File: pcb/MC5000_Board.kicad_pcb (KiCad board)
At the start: 2 copper layers, 100 x 97.5 mm, 127 parts, among them J1 USB_B_Micro, J14 Conn_01x04_Female, J15 Conn_01x04_Female, J16 Conn_01x04_Female, J17 Conn_01x04_Female, J18 Conn_01x04_Female, J19 Conn_01x04_Female, J2 Conn_01x04_Male, J20 Conn_01x04_Female, J21 Conn_01x04_Female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

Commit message: Fabrication stuff
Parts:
- BZ1: footprint Buzzer_Beeper:MagneticBuzzer_CUI_CMT-8504-100-SMT -> LCSC_parts:MagneticBuzzer_7.5x7.5_SMT

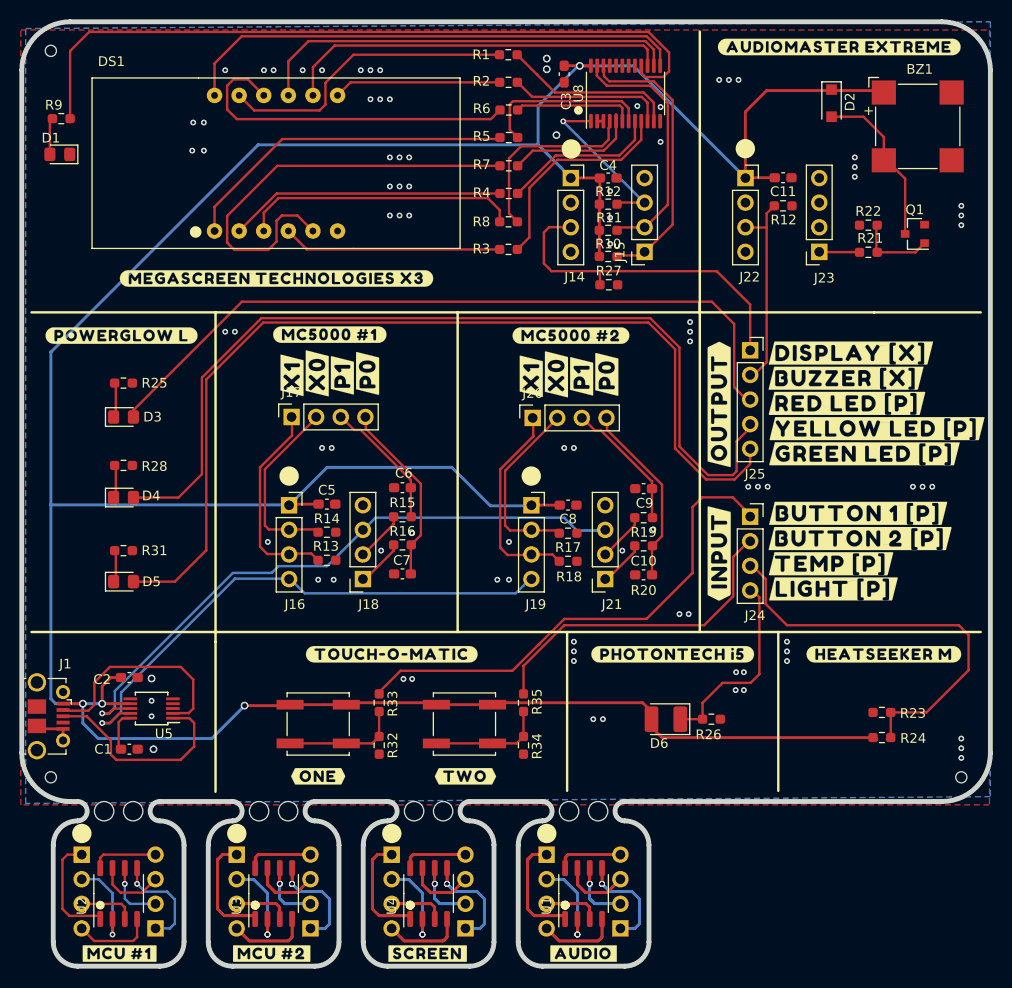
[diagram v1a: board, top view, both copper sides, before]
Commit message: Footprint changes
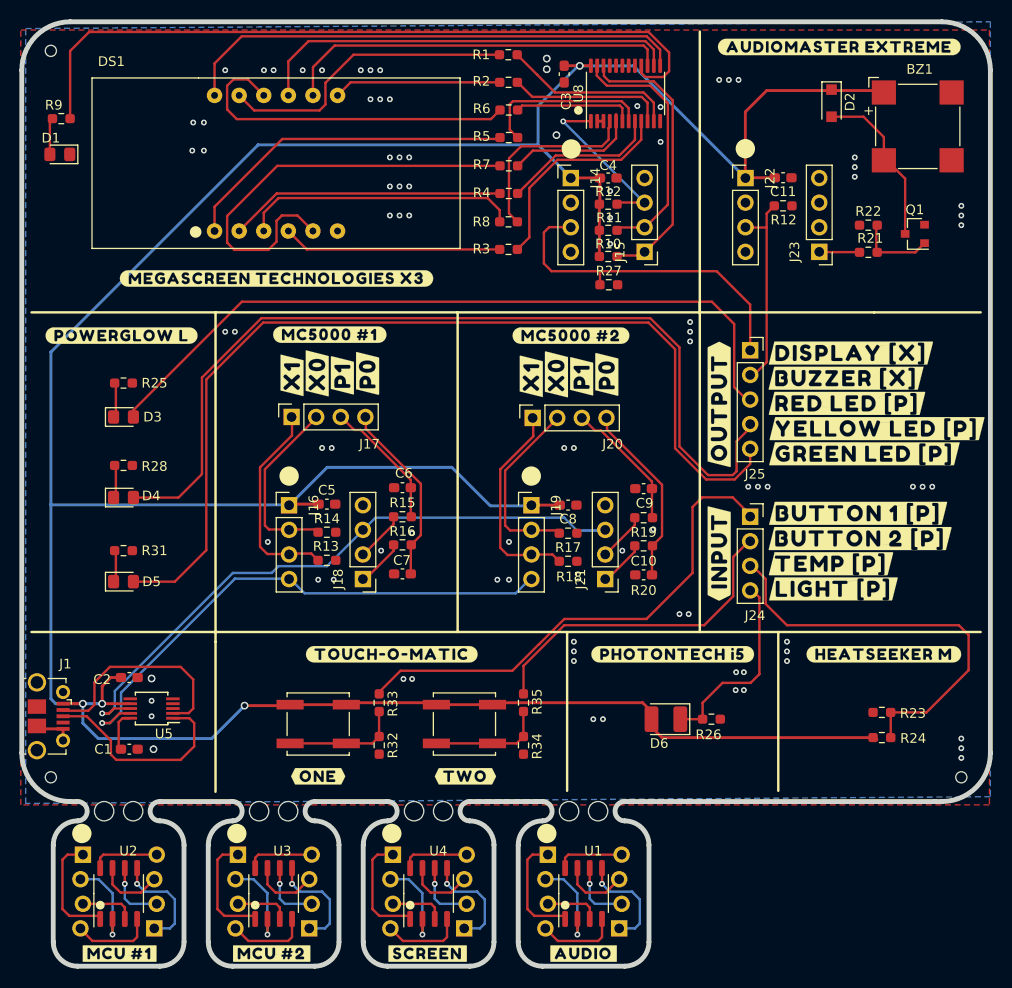
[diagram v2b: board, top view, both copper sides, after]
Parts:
- J14, J15, J16, J18, J19, J21, J22, J23: footprint LCSC_parts:PinSocket_1x04_P2.54mm_Vertical_centered -> LCSC_parts:PinHeader_1x04_P2.54mm_Vertical_centered
- J2, J3, J4, J5, J6, J7, J8, J9: footprint LCSC_parts:PinHeader_1x04_P2.54mm_Vertical_centered -> LCSC_parts:PinHeader_1x04_P2.54mm_plug
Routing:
- net Net-(J8-Pad1): track 35.4 -> 11.8 mm
- net Net-(J6-Pad1): track 35.4 -> 11.8 mm
- net Net-(J2-Pad1): track 35.4 -> 11.8 mm
- net Net-(J9-Pad1): track 33.0 -> 11.0 mm, vias 3 -> 1
- net Net-(J7-Pad1): track 33.0 -> 11.0 mm, vias 3 -> 1
- net Net-(J3-Pad1): track 33.0 -> 11.0 mm, vias 3 -> 1
- net Net-(J8-Pad2): track 29.0 -> 9.66 mm, vias 3 -> 1
- net Net-(J6-Pad2): track 29.0 -> 9.66 mm, vias 3 -> 1
- net Net-(J2-Pad2): track 29.0 -> 9.66 mm, vias 3 -> 1
- net Net-(J6-Pad4): track 24.9 -> 8.34 mm
- net Net-(J8-Pad4): track 24.9 -> 8.37 mm
- net Net-(J2-Pad4): track 24.9 -> 8.37 mm
- net Net-(J9-Pad3): track 21.1 -> 7.04 mm
- net Net-(J7-Pad3): track 21.1 -> 7.04 mm
- net Net-(J3-Pad3): track 21.1 -> 7.04 mm
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
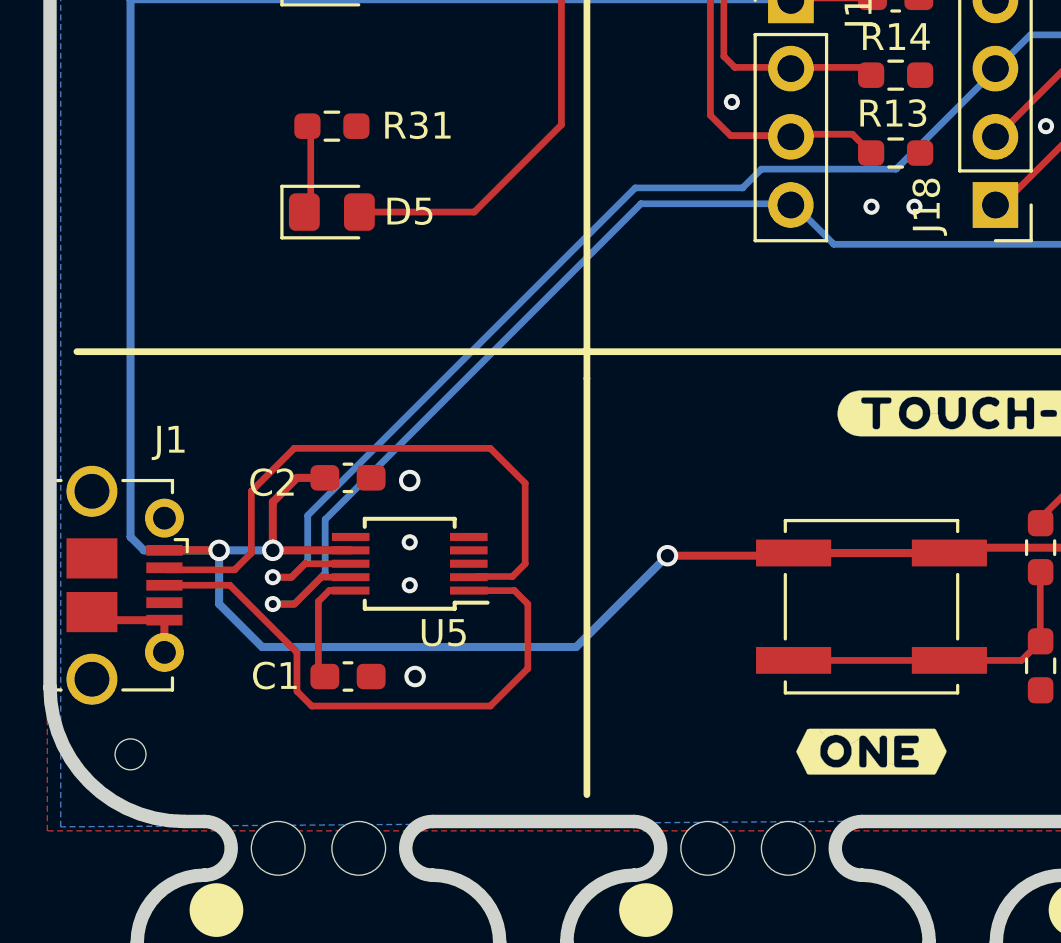
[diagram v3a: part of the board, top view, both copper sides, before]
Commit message: Changed USB<->Serial to CH340G
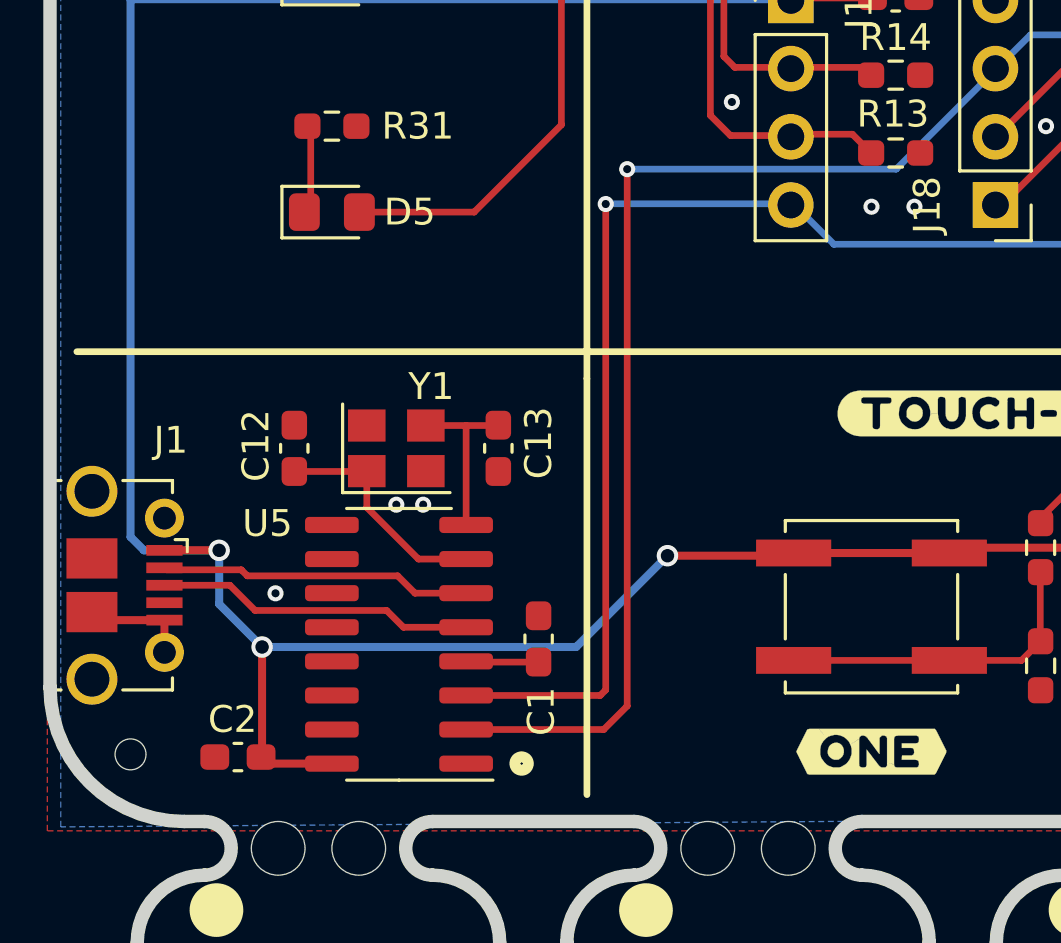
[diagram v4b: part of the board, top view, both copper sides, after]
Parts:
- added C12: 33pF, Capacitor_SMD:C_0603_1608Metric_Pad1.08x0.95mm_HandSolder, F.Cu at (59.1, 106.6)
- added C13: 33pF, Capacitor_SMD:C_0603_1608Metric_Pad1.08x0.95mm_HandSolder, F.Cu at (66.7, 106.6)
- added Y1: Crystal_GND24, Crystal:Crystal_SMD_3225-4Pin_3.2x2.5mm, F.Cu at (62.9, 106.6)
- U5: value CH340E -> CH340G; footprint LCSC_parts:MSOP-10_3x3mm_P0.5mm_rotated -> LCSC_parts:SOP-16_3.9x9.9mm_P1.27mm_rotated
- moved C2 11.2 mm to (57.0, 118.1), turned to 0 degrees
- moved C1 7.24 mm to (68.2, 113.7), turned to 270 degrees
- moved U5 3.03 mm to (63.0, 113.9)
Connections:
- U5 pad 1: Net-(J1-Pad3) -> GND
- U5 pad 10: Net-(C1-Pad2) -> (no net)
- U5 pad 2: Net-(J1-Pad2) -> TXD
- U5 pad 3: GND -> RXD
- U5 pad 4: Net-(U5-Pad4) -> Net-(C1-Pad2)
- U5 pad 5: Net-(U5-Pad5) -> Net-(J1-Pad3)
- U5 pad 6: Net-(U5-Pad6) -> Net-(J1-Pad2)
- U5 pad 7: VCC -> Net-(C12-Pad1)
- U5 pad 8: TXD -> Net-(C13-Pad2)
- U5 pad 9: RXD -> (no net)
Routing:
- net Net-(J1-Pad2): track 22.5 -> 11.6 mm
- net Net-(J1-Pad3): track 21.6 -> 11.9 mm
- net Net-(C12-Pad1): track 0.00 -> 8.55 mm
- net Net-(C13-Pad2): track 0.00 -> 6.41 mm
- net TXD: track 64.9 -> 67.7 mm
- net VCC: track 334.0 -> 331.8 mm
- net Net-(C1-Pad2): track 4.26 -> 2.71 mm
- net GND: vias 90 -> 89

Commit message: Design changes
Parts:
- moved REF** 6.00 mm to (147.0, 124.0)
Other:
- outline, holes or cut-outs redrawn
- board text added: "DevKit V1.0"
- board text added: "MC5000"

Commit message: Added OSHW logo
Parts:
- added REF**: OSHW-Logo_7.5x8mm_SilkScreen, Symbol:OSHW-Logo_7.5x8mm_SilkScreen, F.Cu at (145.1, 115.3)
- moved R23 0.40 mm to (138.8, 110.9)
